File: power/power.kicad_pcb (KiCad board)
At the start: 2 copper layers, 69 parts, among them J1 Conn_01x02_Female, J10 Conn_01x02_Female, J11 Conn_01x02_Female, J12 Conn_01x02_Female, J13 Conn_01x02_Female, J14 Conn_01x02_Female, J15 Conn_01x02_Female, J2 Conn_01x02_Female, J3 CONN_02X03, J4 Conn_01x02_Female, J5 Conn_01x02_Female, J6 Conn_01x02_Female, J7 Conn_01x02_Female, J8 Conn_01x02_Female, J9 Conn_01x02_Female, Q1 BS170, Q11 BS170, Q12 BSB014N04LX3, Q2 BS170, Q3 BS170, Q5 BS170, Q6 BS170, Q7 BS170, U1 MAX1648, U2 TPS2592xx, U3 ATMEGA16M1, U4 LP5907MFX-3_3_NOPB

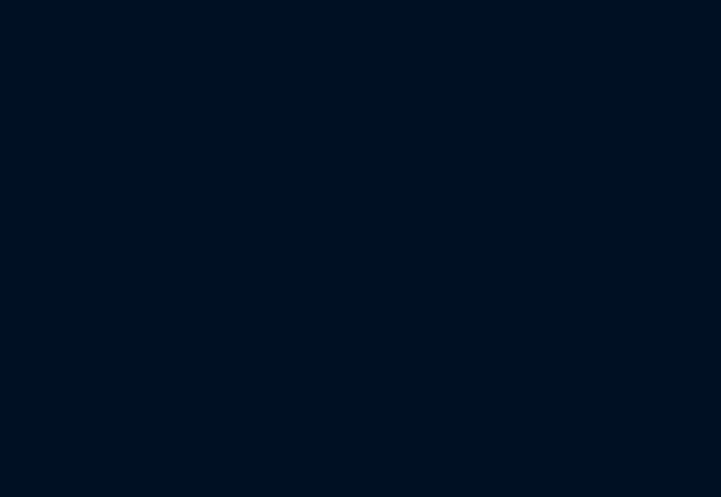
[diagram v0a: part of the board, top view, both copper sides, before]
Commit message: thermistor footprint
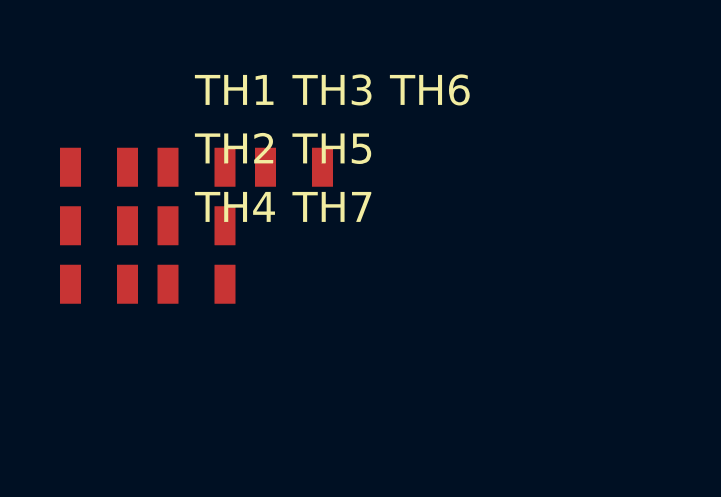
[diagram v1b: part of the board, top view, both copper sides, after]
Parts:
- added TH1: Thermistor, footprints:Thermistor, F.Cu at (21.5, 16.5)
- added TH2: Thermistor, footprints:Thermistor, F.Cu at (21.5, 18.4)
- added TH3: Thermistor, footprints:Thermistor, F.Cu at (24.7, 16.5)
- added TH4: Thermistor, footprints:Thermistor, F.Cu at (21.5, 20.4)
- added TH5: Thermistor, footprints:Thermistor, F.Cu at (24.7, 18.4)
- added TH6: Thermistor, footprints:Thermistor, F.Cu at (28.0, 16.5)
- added TH7: Thermistor, footprints:Thermistor, F.Cu at (24.7, 20.4)
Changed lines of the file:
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@@
     (tracks 8)
     (zones 0)
-    (modules 69)
+    (modules 76)
     (nets 69)
   )
@@
     )
   )
+  (module footprints:Thermistor (layer F.Cu)
+    (at 21.492881 16.453761)
+    (fp_text reference TH1 (at 4.572 -2.54) (layer F.SilkS)
+      (effects (font (size 1 1) (thickness 0.15)))
+    )
+    (fp_text value Thermistor (at -1.778 -2.54) (layer F.Fab)
+      (effects (font (size 1 1) (thickness 0.15)))
+    )
+    (fp_line (start 1 -0.62) (end -1 -0.62) (layer F.Fab) (width 0.15))
+    (fp_line (start -1 0.62) (end 1 0.62) (layer F.Fab) (width 0.15))
+    (fp_line (start -1.55 -0.9) (end 1.55 -0.9) (layer F.Fab) (width 0.15))
+    (fp_line (start 1.55 -0.9) (end 1.55 0.9) (layer F.Fab) (width 0.15))
+    (fp_line (start 1.524 0.9) (end -1.524 0.9) (layer F.Fab) (width 0.15))
+    (fp_line (start -1.55 -0.9) (end -1.55 0.9) (layer F.Fab) (width 0.15))
+    (pad 1 smd rect (at -0.95 0) (size 0.7 1.3) (layers F.Cu F.Paste F.Mask)
+      (net 21 /B1A+))
+    (pad 2 smd rect (at 0.95 0) (size 0.7 1.3) (layers F.Cu F.Paste F.Mask)
+      (net 42 /V1A))
+  )
+  (module footprints:Thermistor (layer F.Cu)
+    (at 21.492881 18.403761)
+    (fp_text reference TH2 (at 4.572 -2.54) (layer F.SilkS)
+      (effects (font (size 1 1) (thickness 0.15)))
+    )
+    (fp_text value Thermistor (at -1.778 -2.54) (layer F.Fab)
+      (effects (font (size 1 1) (thickness 0.15)))
+    )
+    (fp_line (start -1.55 -0.9) (end -1.55 0.9) (layer F.Fab) (width 0.15))
+    (fp_line (start 1.524 0.9) (end -1.524 0.9) (layer F.Fab) (width 0.15))
+    (fp_line (start 1.55 -0.9) (end 1.55 0.9) (layer F.Fab) (width 0.15))
+    (fp_line (start -1.55 -0.9) (end 1.55 -0.9) (layer F.Fab) (width 0.15))
+    (fp_line (start -1 0.62) (end 1 0.62) (layer F.Fab) (width 0.15))
+    (fp_line (start 1 -0.62) (end -1 -0.62) (layer F.Fab) (width 0.15))
+    (pad 2 smd rect (at 0.95 0) (size 0.7 1.3) (layers F.Cu F.Paste F.Mask)
+      (net 41 /V2A))
+    (pad 1 smd rect (at -0.95 0) (size 0.7 1.3) (layers F.Cu F.Paste F.Mask)
+      (net 17 /B1A-))
+  )
+  (module footprints:Thermistor (layer F.Cu)
+    (at 24.742881 16.453761)
+    (fp_text reference TH3 (at 4.572 -2.54) (layer F.SilkS)
+      (effects (font (size 1 1) (thickness 0.15)))
+    )
+    (fp_text value Thermistor (at -1.778 -2.54) (layer F.Fab)
+      (effects (font (size 1 1) (thickness 0.15)))
+    )
+    (fp_line (start 1 -0.62) (end -1 -0.62) (layer F.Fab) (width 0.15))
+    (fp_line (start -1 0.62) (end 1 0.62) (layer F.Fab) (width 0.15))
+    (fp_line (start -1.55 -0.9) (end 1.55 -0.9) (layer F.Fab) (width 0.15))
+    (fp_line (start 1.55 -0.9) (end 1.55 0.9) (layer F.Fab) (width 0.15))
+    (fp_line (start 1.524 0.9) (end -1.524 0.9) (layer F.Fab) (width 0.15))
+    (fp_line (start -1.55 -0.9) (end -1.55 0.9) (layer F.Fab) (width 0.15))
+    (pad 1 smd rect (at -0.95 0) (size 0.7 1.3) (layers F.Cu F.Paste F.Mask)
+      (net 18 /B2A-))
+    (pad 2 smd rect (at 0.95 0) (size 0.7 1.3) (layers F.Cu F.Paste F.Mask)
+      (net 43 /V3A))
+  )
+  (module footprints:Thermistor (layer F.Cu)
+    (at 21.492881 20.353761)
+    (fp_text reference TH4 (at 4.572 -2.54) (layer F.SilkS)
+      (effects (font (size 1 1) (thickness 0.15)))
+    )
+    (fp_text value Thermistor (at -1.778 -2.54) (layer F.Fab)
+      (effects (font (size 1 1) (thickness 0.15)))
+    )
+    (fp_line (start 1 -0.62) (end -1 -0.62) (layer F.Fab) (width 0.15))
+    (fp_line (start -1 0.62) (end 1 0.62) (layer F.Fab) (width 0.15))
+    (fp_line (start -1.55 -0.9) (end 1.55 -0.9) (layer F.Fab) (width 0.15))
+    (fp_line (start 1.55 -0.9) (end 1.55 0.9) (layer F.Fab) (width 0.15))
+    (fp_line (start 1.524 0.9) (end -1.524 0.9) (layer F.Fab) (width 0.15))
+    (fp_line (start -1.55 -0.9) (end -1.55 0.9) (layer F.Fab) (width 0.15))
+    (pad 1 smd rect (at -0.95 0) (size 0.7 1.3) (layers F.Cu F.Paste F.Mask)
+      (net 39 "Net-(R13-Pad1)"))
+    (pad 2 smd rect (at 0.95 0) (size 0.7 1.3) (layers F.Cu F.Paste F.Mask)
+      (net 2 GND))
+  )
+  (module footprints:Thermistor (layer F.Cu)
+    (at 24.742881 18.403761)
+    (fp_text reference TH5 (at 4.572 -2.54) (layer F.SilkS)
+      (effects (font (size 1 1) (thickness 0.15)))
+    )
+    (fp_text value Thermistor (at -1.778 -2.54) (layer F.Fab)
+      (effects (font (size 1 1) (thickness 0.15)))
+    )
+    (fp_line (start -1.55 -0.9) (end -1.55 0.9) (layer F.Fab) (width 0.15))
+    (fp_line (start 1.524 0.9) (end -1.524 0.9) (layer F.Fab) (width 0.15))
+    (fp_line (start 1.55 -0.9) (end 1.55 0.9) (layer F.Fab) (width 0.15))
+    (fp_line (start -1.55 -0.9) (end 1.55 -0.9) (layer F.Fab) (width 0.15))
+    (fp_line (start -1 0.62) (end 1 0.62) (layer F.Fab) (width 0.15))
+    (fp_line (start 1 -0.62) (end -1 -0.62) (layer F.Fab) (width 0.15))
+    (pad 2 smd rect (at 0.95 0) (size 0.7 1.3) (layers F.Cu F.Paste F.Mask)
+      (net 45 /V1B))
+    (pad 1 smd rect (at -0.95 0) (size 0.7 1.3) (layers F.Cu F.Paste F.Mask)
+      (net 1 /B1B+))
+  )
+  (module footprints:Thermistor (layer F.Cu)
+    (at 27.992881 16.453761)
+    (fp_text reference TH6 (at 4.572 -2.54) (layer F.SilkS)
+      (effects (font (size 1 1) (thickness 0.15)))
+    )
+    (fp_text value Thermistor (at -1.778 -2.54) (layer F.Fab)
+      (effects (font (size 1 1) (thickness 0.15)))
+    )
+    (fp_line (start 1 -0.62) (end -1 -0.62) (layer F.Fab) (width 0.15))
+    (fp_line (start -1 0.62) (end 1 0.62) (layer F.Fab) (width 0.15))
+    (fp_line (start -1.55 -0.9) (end 1.55 -0.9) (layer F.Fab) (width 0.15))
+    (fp_line (start 1.55 -0.9) (end 1.55 0.9) (layer F.Fab) (width 0.15))
+    (fp_line (start 1.524 0.9) (end -1.524 0.9) (layer F.Fab) (width 0.15))
+    (fp_line (start -1.55 -0.9) (end -1.55 0.9) (layer F.Fab) (width 0.15))
+    (pad 1 smd rect (at -0.95 0) (size 0.7 1.3) (layers F.Cu F.Paste F.Mask)
+      (net 19 /B1B-))
+    (pad 2 smd rect (at 0.95 0) (size 0.7 1.3) (layers F.Cu F.Paste F.Mask)
+      (net 46 /V2B))
+  )
+  (module footprints:Thermistor (layer F.Cu)
+    (at 24.742881 20.353761)
+    (fp_text reference TH7 (at 4.572 -2.54) (layer F.SilkS)
+      (effects (font (size 1 1) (thickness 0.15)))
+    )
+    (fp_text value Thermistor (at -1.778 -2.54) (layer F.Fab)
+      (effects (font (size 1 1) (thickness 0.15)))
+    )
+    (fp_line (start -1.55 -0.9) (end -1.55 0.9) (layer F.Fab) (width 0.15))
+    (fp_line (start 1.524 0.9) (end -1.524 0.9) (layer F.Fab) (width 0.15))
+    (fp_line (start 1.55 -0.9) (end 1.55 0.9) (layer F.Fab) (width 0.15))
+    (fp_line (start -1.55 -0.9) (end 1.55 -0.9) (layer F.Fab) (width 0.15))
+    (fp_line (start -1 0.62) (end 1 0.62) (layer F.Fab) (width 0.15))
+    (fp_line (start 1 -0.62) (end -1 -0.62) (layer F.Fab) (width 0.15))
+    (pad 2 smd rect (at 0.95 0) (size 0.7 1.3) (layers F.Cu F.Paste F.Mask)
+      (net 47 /V3B))
+    (pad 1 smd rect (at -0.95 0) (size 0.7 1.3) (layers F.Cu F.Paste F.Mask)
+      (net 20 /B2B-))
+  )
   (segment (start 64.37376 118.14124) (end 64.20612 118.30888) (width 0.25) (layer F.Cu) (net 17))

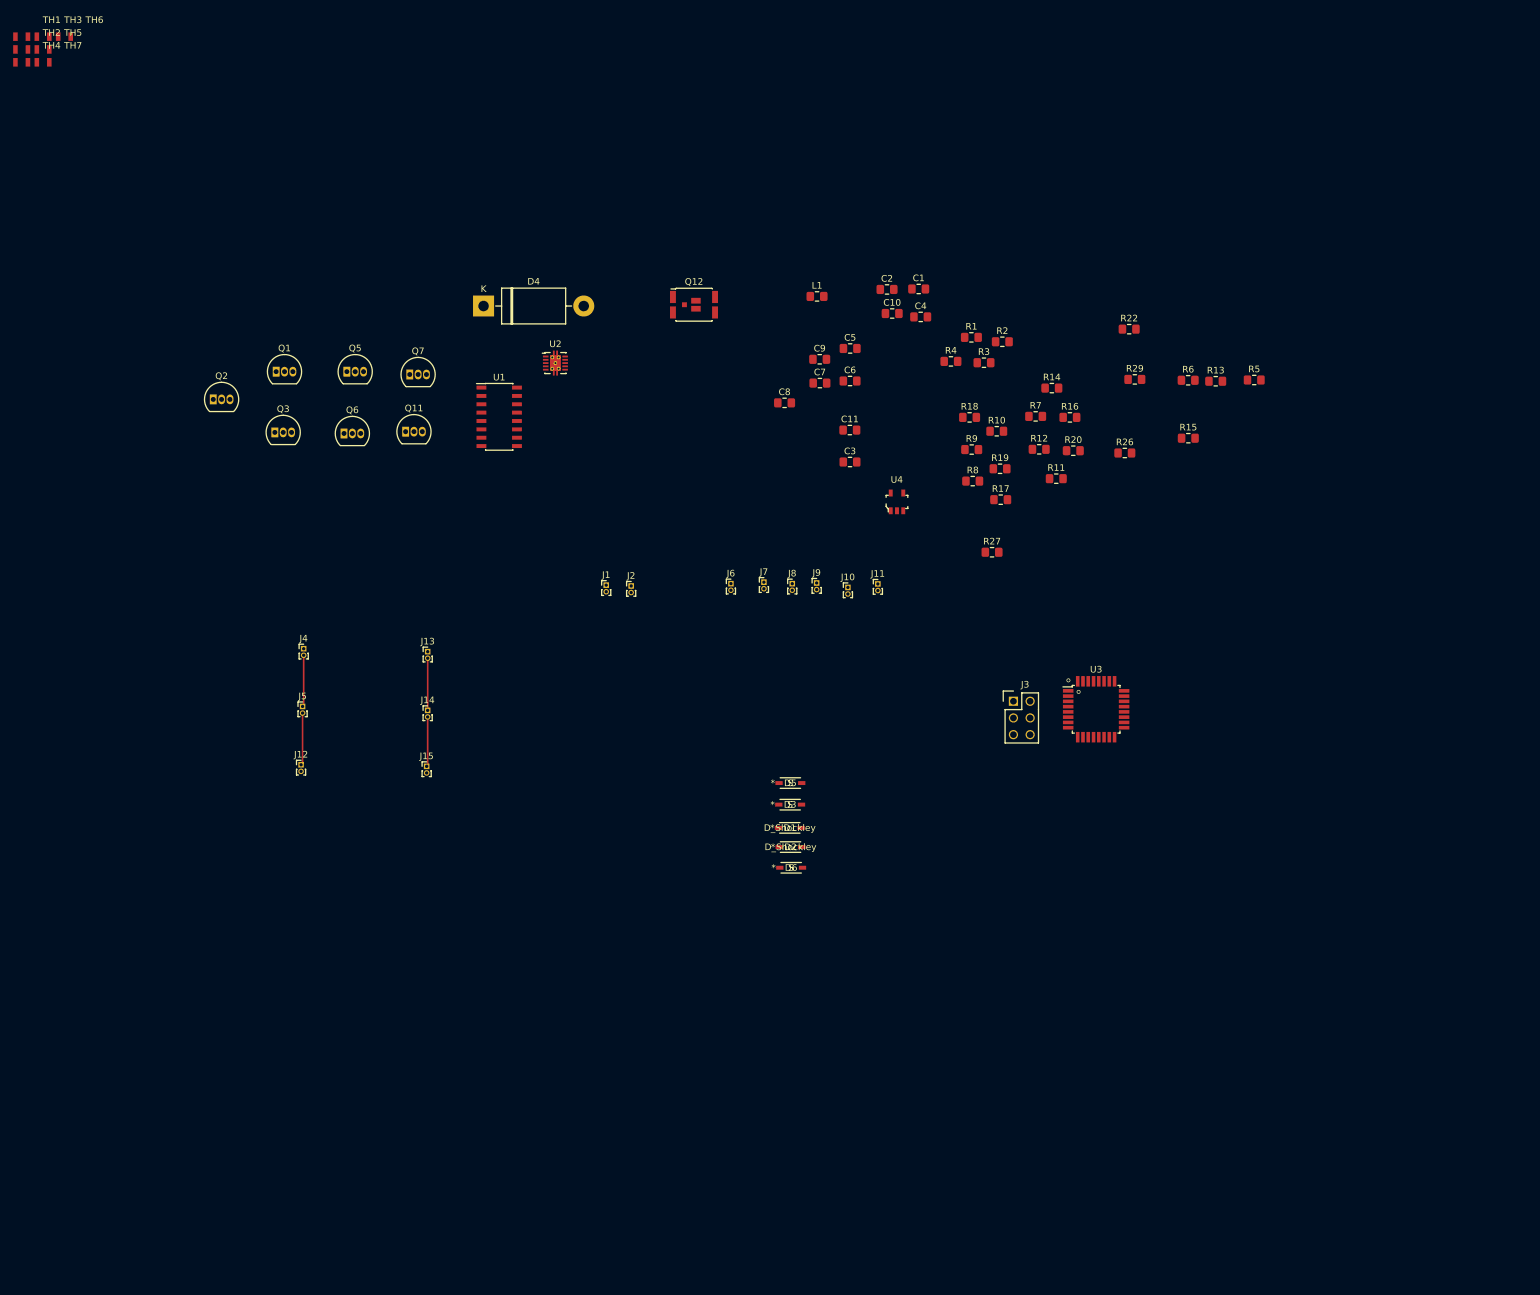
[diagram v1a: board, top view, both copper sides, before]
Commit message: separated charging from main board
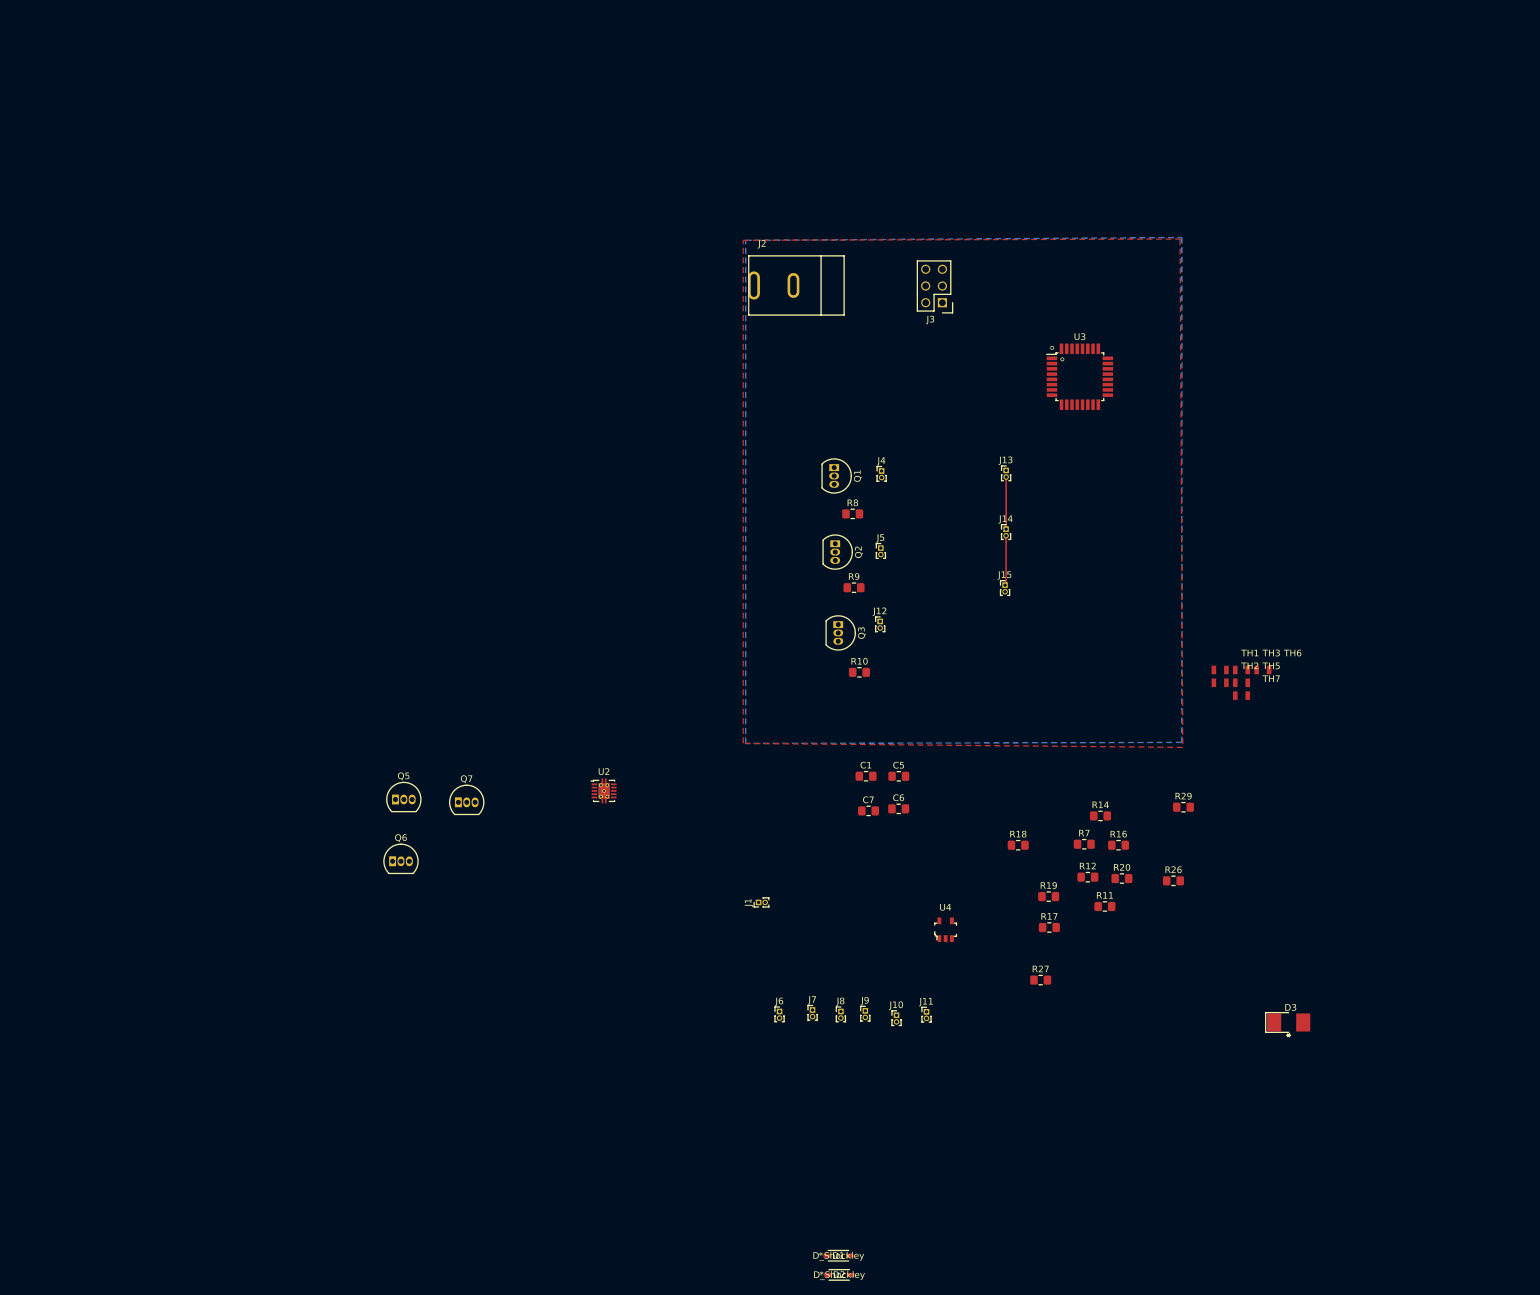
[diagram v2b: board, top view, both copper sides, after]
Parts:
- removed C10, C2, C4: 0.1uF, Capacitor_SMD:C_0805_2012Metric_Pad1.15x1.40mm_HandSolder
- removed C11: 47uF, Capacitor_SMD:C_0805_2012Metric_Pad1.15x1.40mm_HandSolder
- removed C3: 47nF, Capacitor_SMD:C_0805_2012Metric_Pad1.15x1.40mm_HandSolder
- removed C8: 22uF, Capacitor_SMD:C_0805_2012Metric_Pad1.15x1.40mm_HandSolder
- removed C9: 1uF, Capacitor_SMD:C_0805_2012Metric_Pad1.15x1.40mm_HandSolder
- removed D4: UF5400, Diode_THT:D_DO-201AD_P15.24mm_Horizontal
- removed D5, D6: S, footprints:SD103AW-13-F
- removed L1: 22uH, Inductor_SMD:L_0805_2012Metric_Pad1.15x1.40mm_HandSolder
- removed Q11: BS170, Package_TO_SOT_THT:TO-92_Inline
- removed Q12: BSB014N04LX3, Package_DirectFET:DirectFET_MX
- removed R1, R2, R3, R4: R, Resistor_SMD:R_0805_2012Metric_Pad1.15x1.40mm_HandSolder
- removed R13, R5, R6: 10k, Resistor_SMD:R_0805_2012Metric_Pad1.15x1.40mm_HandSolder
- removed R15: 10, Resistor_SMD:R_0805_2012Metric_Pad1.15x1.40mm_HandSolder
- removed R22: 0.74, Resistor_SMD:R_0805_2012Metric_Pad1.15x1.40mm_HandSolder
- removed TH4: Thermistor, footprints:Thermistor
- removed U1: MAX1648, Package_SO:SOIC-16_3.9x9.9mm_P1.27mm
- D3: value S -> D_Zener_13V; footprint footprints:SD103AW-13-F -> footprints:D_13V_Zener
- J2: value Conn_01x02_Female -> Barrel_jack; footprint Connector_PinHeader_1.00mm:PinHeader_1x02_P1.00mm_Vertical -> footprints:barrel_jack_PJ-037A
- moved TH1 206.1 mm to (203.7, 112.8)
- moved TH2 206.1 mm to (203.7, 114.7)
- moved TH3 206.1 mm to (207.0, 112.8)
- moved TH5 206.1 mm to (207.0, 114.7)
- moved TH6 206.1 mm to (210.2, 112.8)
- moved TH7 206.1 mm to (207.0, 116.7)
- moved Q2 97.1 mm to (145.2, 93.6), turned to 270 degrees
- moved J14 92.2 mm to (171.2, 91.3)
- moved J15 92.2 mm to (171.0, 99.9)
- moved J13 92.2 mm to (171.2, 82.4)
- moved J4 92.0 mm to (152.3, 82.5)
- moved J5 91.2 mm to (152.1, 94.2)
- moved J12 90.7 mm to (152.0, 105.4)
- moved Q3 90.5 mm to (145.7, 105.9), turned to 270 degrees
- moved Q1 86.1 mm to (145.0, 82.0), turned to 270 degrees
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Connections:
- net /Discharge renamed Net-(U3-Pad2)
- net /SafetySwitchA renamed Net-(U3-Pad30)
- net /SafetySwitchB renamed Net-(U3-Pad22)
- D1 pad 2: Net-(D1-Pad2) -> /BAT+
- D3 pad 1: Net-(C10-Pad2) -> /B1B+
- J2 pad 1: /DC+ -> /BAT+
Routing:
- net /B2A-: track 7.96 -> 0.00 mm
- net /B1A-: track 7.85 -> 0.00 mm
- added copper zone on F.Cu, net +12V
- added copper zone on B.Cu, net GND

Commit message: half layout
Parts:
- moved D2 140.6 mm to (176.3, 67.5), turned to 180 degrees
- moved D1 140.2 mm to (135.5, 62.0), turned to 180 degrees
- moved Q5 117.1 mm to (178.4, 71.6), turned to 270 degrees
- moved Q6 116.5 mm to (178.4, 82.9), turned to 270 degrees
- moved J10 114.1 mm to (179.0, 53.9), turned to 180 degrees
- moved J11 113.7 mm to (184.1, 53.8), turned to 180 degrees
- moved J9 113.4 mm to (174.0, 53.8), turned to 180 degrees
- moved J8 113.1 mm to (168.6, 53.8), turned to 180 degrees
- moved J6 112.9 mm to (157.7, 53.8), turned to 180 degrees
- moved J7 112.7 mm to (162.9, 53.8), turned to 180 degrees
- moved Q7 98.1 mm to (178.4, 95.2), turned to 270 degrees
- moved J1 96.1 mm to (152.4, 53.8), turned to 180 degrees
- moved U4 94.8 mm to (189.4, 61.6), turned to 90 degrees
- moved D3 94.5 mm to (194.9, 73.9), turned to 270 degrees
- moved R11 88.2 mm to (148.3, 69.0)
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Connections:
- U3 pad 1: /FET2B -> /FET1A
- U3 pad 23: /FET3A -> /FET2B
- U3 pad 6: /FET1A -> /FET3A
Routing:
- net /B1A+: track 0.00 -> 43.6 mm
- net GND: track 0.00 -> 31.7 mm, vias 0 -> 8
- net /FET3A: track 0.00 -> 25.2 mm
- net /FET1A: track 0.00 -> 23.2 mm
- net /B1A-: track 0.00 -> 23.0 mm
- net /B2A-: track 0.00 -> 22.2 mm
- net /FET2A: track 0.00 -> 20.1 mm
- net Net-(Q2-Pad3): track 0.00 -> 17.1 mm
- net Net-(Q1-Pad3): track 0.00 -> 15.8 mm
- net /BAT+: track 0.00 -> 8.22 mm
- net /B1B-: track 7.93 -> 0.00 mm
- net /B2B-: track 7.58 -> 0.00 mm
- net Net-(Q3-Pad3): track 0.00 -> 4.02 mm
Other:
- board text added: "+"
- board text added: "Baro1"
- board text added: "Baro2"
- board text added: "GPS"
- board text added: "IMU"
- board text added: "Radio"
- board text added: "Recovery"
- board text added: "Teensy"
